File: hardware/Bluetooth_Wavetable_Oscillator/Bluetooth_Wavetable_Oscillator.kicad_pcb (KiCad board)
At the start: 2 copper layers, 4 parts, among them J2 AWHW2 10G-0202, U2 ESP32-DEVKITC-32D

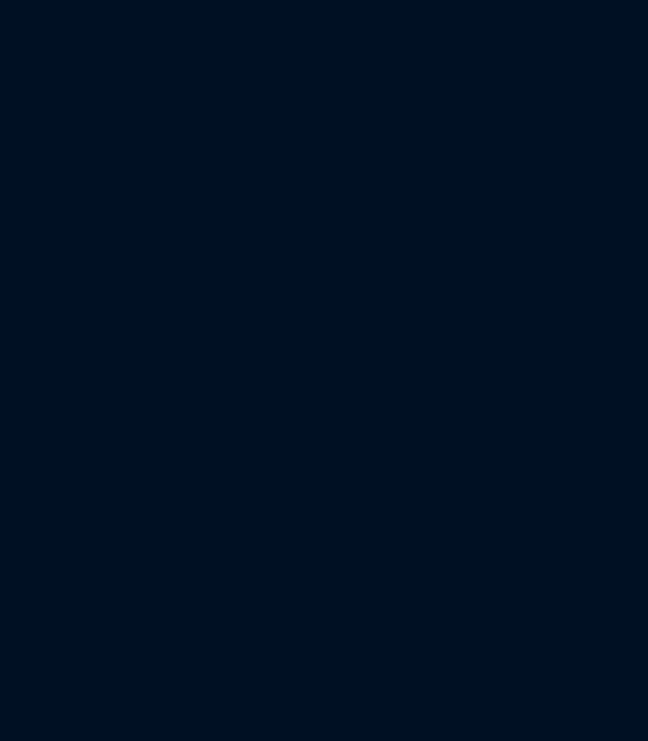
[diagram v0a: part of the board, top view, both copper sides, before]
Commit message: add audio test files
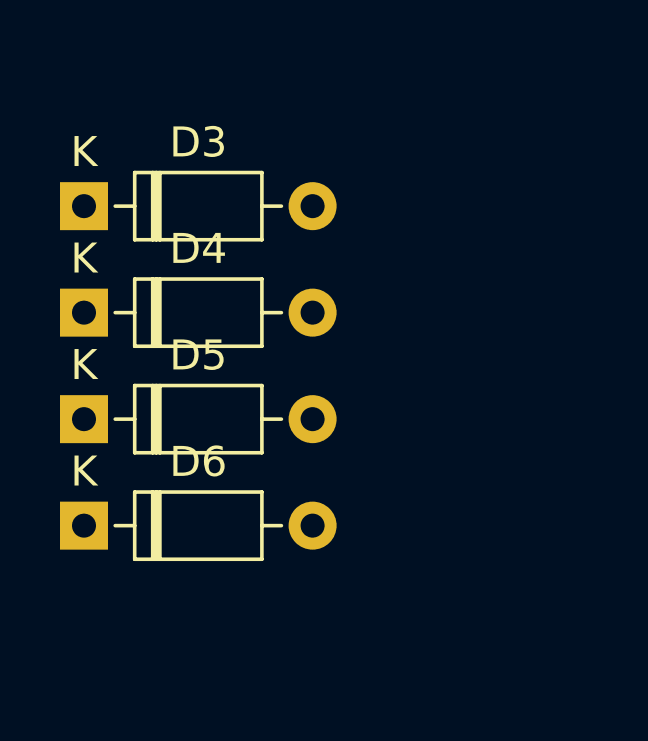
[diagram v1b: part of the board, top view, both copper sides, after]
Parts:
- added D3: BAT48RL, Diode_THT:D_DO-35_SOD27_P7.62mm_Horizontal, F.Cu at (37.1, 38.7)
- added D4: BAT48RL, Diode_THT:D_DO-35_SOD27_P7.62mm_Horizontal, F.Cu at (37.1, 42.2)
- added D5: BAT48RL, Diode_THT:D_DO-35_SOD27_P7.62mm_Horizontal, F.Cu at (37.1, 45.8)
- added D6: BAT48RL, Diode_THT:D_DO-35_SOD27_P7.62mm_Horizontal, F.Cu at (37.1, 49.3)

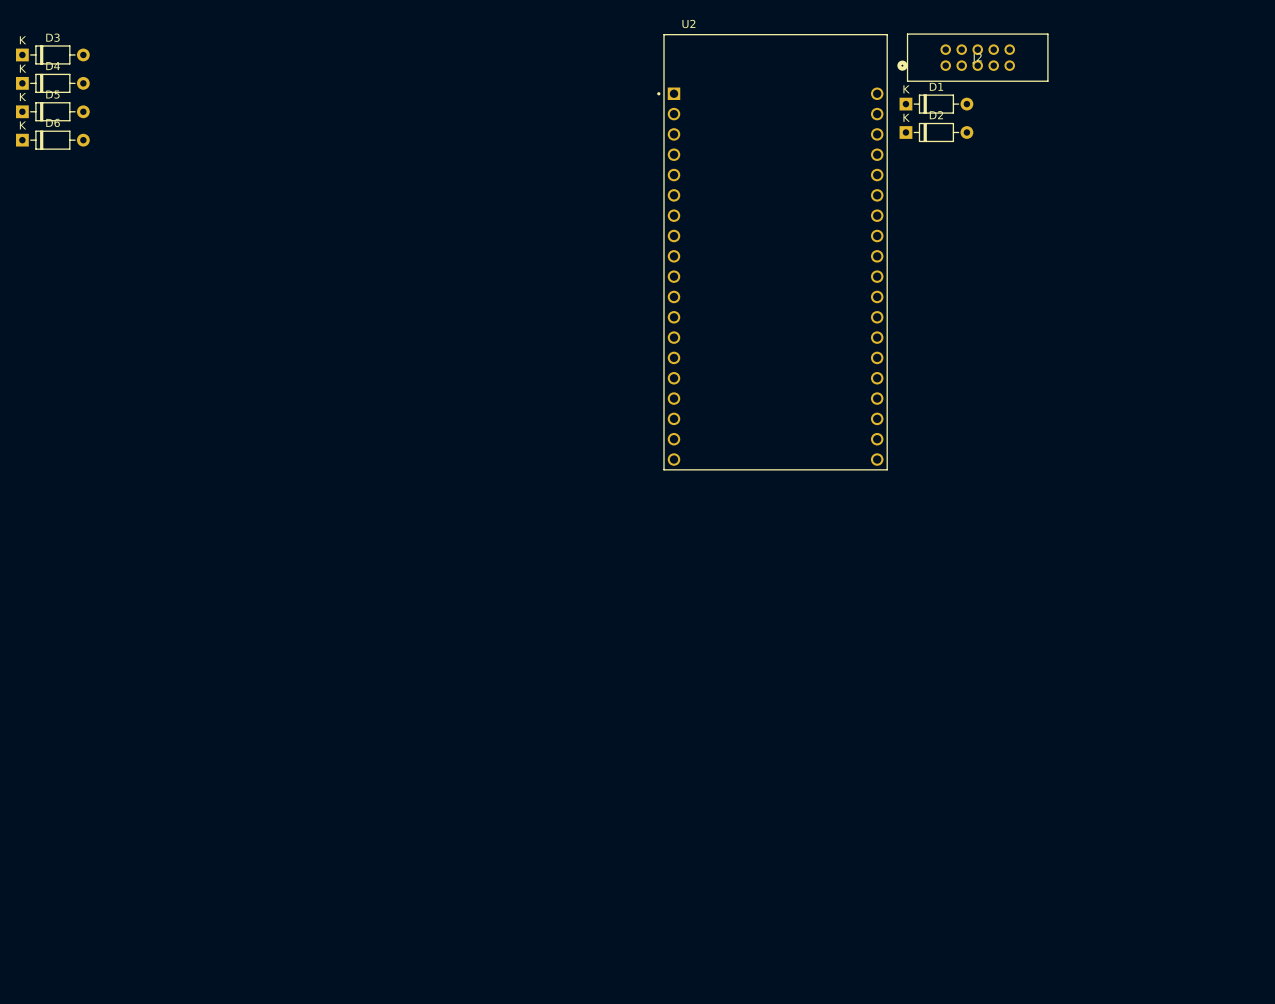
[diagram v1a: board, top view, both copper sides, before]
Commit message: start PCB layout
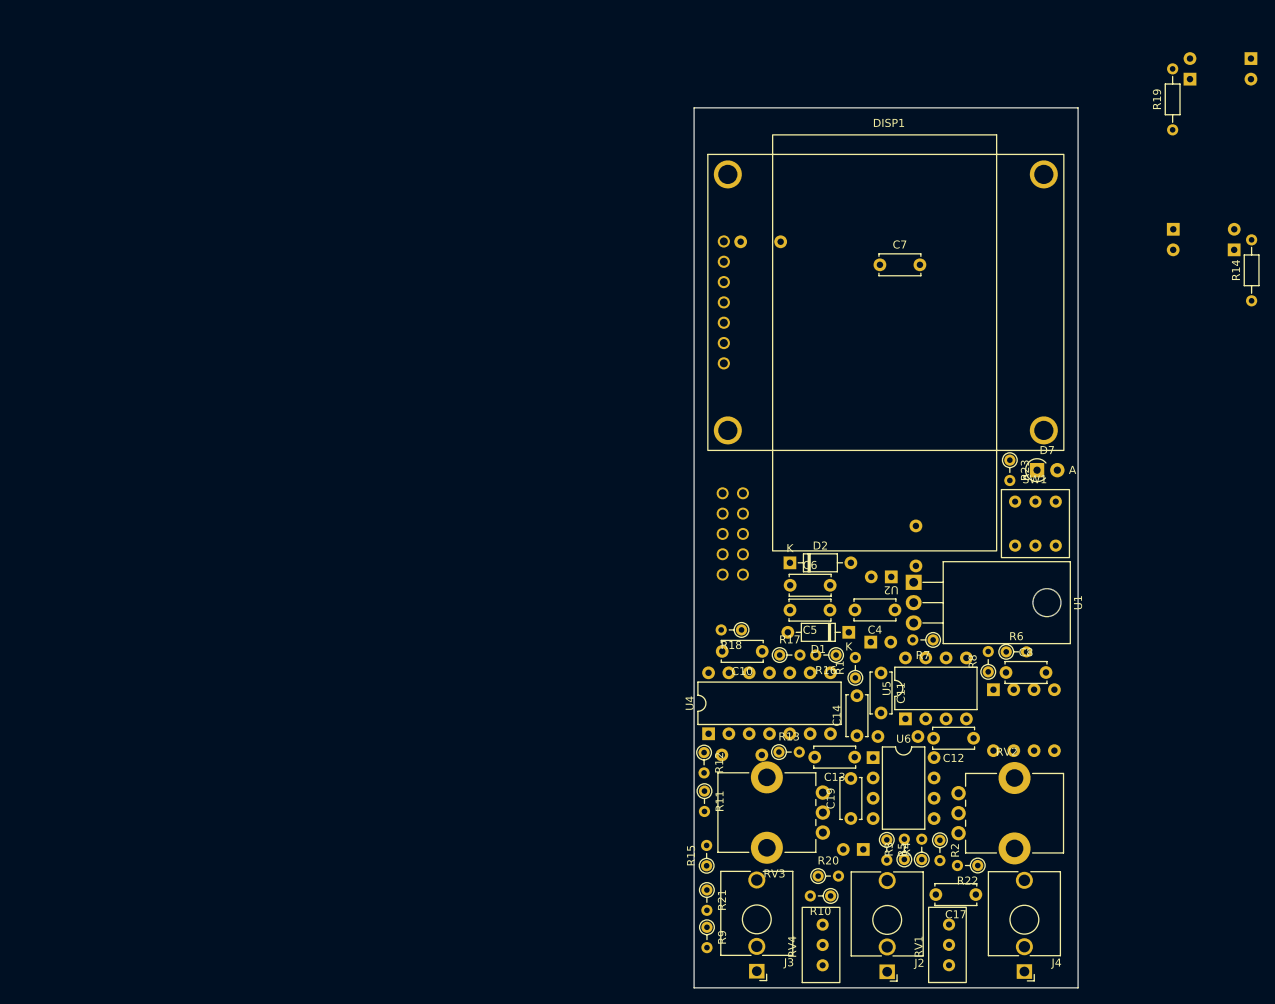
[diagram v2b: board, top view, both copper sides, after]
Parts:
- added C1: 0.33u, Capacitor_THT:C_Disc_D5.0mm_W2.5mm_P5.00mm, B.Cu at (148.8, 102.5)
- added C10: 0.1u, Capacitor_THT:C_Disc_D5.0mm_W2.5mm_P5.00mm, F.Cu at (129.6, 113.2)
- added C11: 0.1u, Capacitor_THT:C_Disc_D5.0mm_W2.5mm_P5.00mm, F.Cu at (144.4, 115.9)
- added C12: 0.1u, Capacitor_THT:C_Disc_D5.0mm_W2.5mm_P5.00mm, F.Cu at (156.0, 124.1)
- added C13: 100p, Capacitor_THT:C_Disc_D5.0mm_W2.5mm_P5.00mm, F.Cu at (141.1, 126.5)
- added C14: 100p, Capacitor_THT:C_Disc_D5.0mm_W2.5mm_P5.00mm, F.Cu at (141.4, 123.8)
- added C15: 0.1u, Capacitor_THT:C_Disc_D5.0mm_W2.5mm_P5.00mm, B.Cu at (131.9, 62.0)
- added C16: 10u, Capacitor_THT:CP_Radial_D5.0mm_P2.50mm, B.Cu at (142.2, 138.0)
- added C17: 0.1u, Capacitor_THT:C_Disc_D5.0mm_W2.5mm_P5.00mm, F.Cu at (156.3, 143.6)
- added C18: 0.1u, Capacitor_THT:C_Disc_D5.0mm_W2.5mm_P5.00mm, B.Cu at (149.0, 123.9)
- added C19: 0.1u, Capacitor_THT:C_Disc_D5.0mm_W2.5mm_P5.00mm, F.Cu at (140.7, 134.1)
- added C2: 47u, Capacitor_THT:CP_Radial_D5.0mm_P2.50mm, B.Cu at (143.1, 112.1)
- added C3: 47u, Capacitor_THT:CP_Radial_D5.0mm_P2.50mm, B.Cu at (145.7, 103.9)
- added C4: 0.1u, Capacitor_THT:C_Disc_D5.0mm_W2.5mm_P5.00mm, F.Cu at (146.2, 108.0)
- added C5: 0.1u, Capacitor_THT:C_Disc_D5.0mm_W2.5mm_P5.00mm, F.Cu at (138.0, 108.1)
- added C6: 0.1u, Capacitor_THT:C_Disc_D5.0mm_W2.5mm_P5.00mm, F.Cu at (133.1, 105.0)
- added C7: 0.1u, Capacitor_THT:C_Disc_D5.0mm_W2.5mm_P5.00mm, F.Cu at (144.3, 64.9)
- added C8: 0.1u, Capacitor_THT:C_Disc_D5.0mm_W2.5mm_P5.00mm, F.Cu at (160.0, 115.9)
- added C9: 0.1u, Capacitor_THT:C_Disc_D5.0mm_W2.5mm_P5.00mm, B.Cu at (129.5, 126.2)
- added D7: LED, Diode_THT:D_A-405_P2.54mm_Vertical_AnodeUp, F.Cu at (163.9, 90.6)
- added DISP1: ~, 1.5inch_RGB_OLED_Module:1.5inch_RGB_OLED_Module, F.Cu at (122.8, 51.1)
- added J1: 2x5 Connector, 10_pin_eurorack_connector:10_pin_eurorack_connector, B.Cu at (125.9, 98.5)
- added J3: AudioJack2_SwitchT, Connector_Audio:Jack_3.5mm_QingPu_WQP-PJ398SM_Vertical_CircularHoles, F.Cu at (128.9, 153.2)
- added J4: AudioJack2_SwitchT, Connector_Audio:Jack_3.5mm_QingPu_WQP-PJ398SM_Vertical_CircularHoles, F.Cu at (162.3, 153.2)
- added R1: 39k, Resistor_THT:R_Axial_DIN0204_L3.6mm_D1.6mm_P2.54mm_Vertical, F.Cu at (141.2, 116.5)
- added R10: 27k, Resistor_THT:R_Axial_DIN0204_L3.6mm_D1.6mm_P2.54mm_Vertical, F.Cu at (138.1, 143.8)
- added R11: 10k, Resistor_THT:R_Axial_DIN0204_L3.6mm_D1.6mm_P2.54mm_Vertical, F.Cu at (122.3, 130.7)
- added R12: 27k, Resistor_THT:R_Axial_DIN0204_L3.6mm_D1.6mm_P2.54mm_Vertical, F.Cu at (122.3, 125.9)
- added R13: 27k, Resistor_THT:R_Axial_DIN0204_L3.6mm_D1.6mm_P2.54mm_Vertical, F.Cu at (131.7, 125.8)
- added R14: 8.2k, Resistor_THT:R_Axial_DIN0204_L3.6mm_D1.6mm_P7.62mm_Horizontal, F.Cu at (190.7, 69.4)
- added R15: 27k, Resistor_THT:R_Axial_DIN0204_L3.6mm_D1.6mm_P2.54mm_Vertical, F.Cu at (122.6, 140.0)
- added R16: 18k, Resistor_THT:R_Axial_DIN0204_L3.6mm_D1.6mm_P2.54mm_Vertical, F.Cu at (138.8, 113.7)
- added R17: 27k, Resistor_THT:R_Axial_DIN0204_L3.6mm_D1.6mm_P2.54mm_Vertical, F.Cu at (131.8, 113.7)
- added R18: 27k, Resistor_THT:R_Axial_DIN0204_L3.6mm_D1.6mm_P2.54mm_Vertical, F.Cu at (127.0, 110.5)
- added R19: 8.2k, Resistor_THT:R_Axial_DIN0204_L3.6mm_D1.6mm_P7.62mm_Horizontal, F.Cu at (180.9, 48.0)
- added R2: 39k, Resistor_THT:R_Axial_DIN0204_L3.6mm_D1.6mm_P2.54mm_Vertical, F.Cu at (151.8, 136.8)
- added R20: 820R, Resistor_THT:R_Axial_DIN0204_L3.6mm_D1.6mm_P2.54mm_Vertical, F.Cu at (136.6, 141.3)
- added R21: 1.8k, Resistor_THT:R_Axial_DIN0204_L3.6mm_D1.6mm_P2.54mm_Vertical, F.Cu at (122.7, 143.1)
- added R22: 1.5k, Resistor_THT:R_Axial_DIN0204_L3.6mm_D1.6mm_P2.54mm_Vertical, F.Cu at (156.5, 140.0)
- added R23: 220R, Resistor_THT:R_Axial_DIN0204_L3.6mm_D1.6mm_P2.54mm_Vertical, F.Cu at (160.5, 89.3)
- added R3: 10k, Resistor_THT:R_Axial_DIN0204_L3.6mm_D1.6mm_P2.54mm_Vertical, F.Cu at (147.3, 139.2)
- added R4: 10k, Resistor_THT:R_Axial_DIN0204_L3.6mm_D1.6mm_P2.54mm_Vertical, F.Cu at (149.5, 139.2)
- added R5: 47k, Resistor_THT:R_Axial_DIN0204_L3.6mm_D1.6mm_P2.54mm_Vertical, F.Cu at (145.1, 136.8)
- added R6: 27k, Resistor_THT:R_Axial_DIN0204_L3.6mm_D1.6mm_P2.54mm_Vertical, F.Cu at (160.1, 113.3)
- added R7: 12k, Resistor_THT:R_Axial_DIN0204_L3.6mm_D1.6mm_P2.54mm_Vertical, F.Cu at (150.9, 111.8)
- added R8: 12k, Resistor_THT:R_Axial_DIN0204_L3.6mm_D1.6mm_P2.54mm_Vertical, F.Cu at (157.8, 115.8)
- added R9: 27k, Resistor_THT:R_Axial_DIN0204_L3.6mm_D1.6mm_P2.54mm_Vertical, F.Cu at (122.7, 147.7)
- added RV1: 10k, Trimmer-potentiometer:Trimmer-potentiometer, F.Cu at (150.4, 154.6)
- added RV2: 10k, Potentiometer_THT:Potentiometer_Bourns_PTV09A-1_Single_Vertical, F.Cu at (154.1, 136.0)
- added RV3: 10k, Potentiometer_THT:Potentiometer_Bourns_PTV09A-1_Single_Vertical, F.Cu at (137.2, 130.9)
- added RV4: 10k, Trimmer-potentiometer:Trimmer-potentiometer, F.Cu at (134.6, 154.6)
- added SW1: SW_Push, 6Pin-Switch-Button:6Pin-Switch-Button, F.Cu at (163.7, 97.3)
- added U1: L7805, Package_TO_SOT_THT:TO-220-3_Horizontal_TabDown, F.Cu at (148.5, 104.6)
- added U3: MCP4821, Package_DIP:DIP-8_W7.62mm, B.Cu at (158.5, 118.0)
- added U4: TL074, Package_DIP:DIP-14_W7.62mm, F.Cu at (122.9, 123.5)
- added U5: TL072, Package_DIP:DIP-8_W7.62mm, F.Cu at (147.5, 121.7)
- added U6: NE5532, Package_DIP:DIP-8_W7.62mm, F.Cu at (143.4, 126.5)
- D1, D2: value BAT48RL -> BAT48
- D3, D4, D5, D6: value BAT48RL -> BAT48; moved to B.Cu
- J2: value AWHW2 10G-0202 -> AudioJack2; footprint footprints:conn10_AWHW2 10G-0202_ASM -> Connector_Audio:Jack_3.5mm_QingPu_WQP-PJ398SM_Vertical_CircularHoles
- U2: value ESP32-DEVKITC-32D -> ESP32-WROOM-32D; footprint ESP32-DEVKITC-32D:MODULE_ESP32-DEVKITC-32D -> ESP32:ESP32
- moved D6 153.9 mm to (190.7, 39.1), turned to 180 degrees
- moved D3 153.4 mm to (188.6, 63.0), turned to 180 degrees
- moved D5 146.0 mm to (183.0, 41.7)
- moved D4 145.0 mm to (180.9, 60.5)
- moved J2 113.5 mm to (145.2, 153.3), turned to 180 degrees
- moved D1 66.4 mm to (140.4, 110.8), turned to 180 degrees
- moved D2 55.7 mm to (133.0, 102.2)
- moved U2 31.3 mm to (158.9, 48.7), turned to 180 degrees
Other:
- board outline added: 48 x 110 mm
